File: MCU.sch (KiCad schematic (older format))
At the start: 27 parts, among them J15 RESET, J16 AVR-ISP-6, J17 WS2812, J18 SJ-43514-SMT, J4 AREF, J7 TYPE-C-31-M-12, SW1 EC11E, U1 ATmega32U4-AU, Y1 CSTNE16M0VH3L000R0

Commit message: Updated symbol library names
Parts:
- U1: symbol MCU_Atmel_ATMEGA:ATmega32U4-AU -> MCU_Microchip_ATmega:ATmega32U4-AU

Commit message: Added CUI connector lib
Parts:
- J16: value AVR-ISP-6 -> ISP
- J18: footprint (none) -> CUI:SJ-43514-SMT; symbol Connector:AudioJack4_Ground -> Connector:AudioJack4
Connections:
- net GND: no longer J18.G

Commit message: Added 3D models, prettied up silk
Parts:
- added D25: BAV70, Diode_SMD:D_SOD-323_HandSoldering, symbol Device:D_Small
- added D27: Red LED, symbol Device:LED_Small
- added R3: 220R, Resistor_SMD:R_0603_1608Metric_Pad1.05x0.95mm_HandSolder, symbol Device:R_Small
- added SW3: Reset, Button_Switch_SMD:SW_SPST_CK_RS282G05A3, symbol Switch:SW_Push
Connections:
- net Enc_A: now also U1.8 (PB0)
- net Enc_B: now also U1.1 (PE6)
- net GND: now also D27.1 (K), SW3.2; no longer SW1.S2
- net WS2812_out: now also U1.30 (PB6)
- net buzz: now also U1.31 (PC6)
- net row0: now also D25.2 (A)
- net ~reset: now also SW3.1
- net Enc_S1: now reaches U1.32 (PC7)
- net Enc_S1: now also SW1.S2
- net Enc_SW: no longer names the net of SW1.S1
- net Enc_SW: now also D25.1 (K)
- new net: D27.2 (A), R3.1
- new net DFU_LED: R3.2
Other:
- moved on the sheet: BZ1, BZ2, R12
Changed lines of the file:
@@
 EESchema Schematic File Version 4
-LIBS:MMboard1-cache
-EELAYER 30 0
+LIBS:mystic_split40-cache
+EELAYER 29 0
 EELAYER END
 $Descr A4 11693 8268
@@
 L Device:Buzzer BZ1
 U 1 1 5DD85748
-P 5175 5550
+P 5200 5925
 AR Path="/5DCB7F8C/5DD85748" Ref="BZ1"  Part="1"
 AR Path="/5E0F7128/5DD85748" Ref="BZ3"  Part="1"
-F 0 "BZ1" H 5328 5579 50  0000 L CNN
-F 1 "Buzzer_magnetic" H 5025 5375 50  0000 L CNN
-F 2 "Buzzer_Beeper:Buzzer_12x9.5RM7.6" V 5150 5650 50  0001 C CNN
-F 3 "~" V 5150 5650 50  0001 C CNN
-	1    5175 5550
+F 0 "BZ1" H 5353 5954 50  0000 L CNN
+F 1 "Buzzer_magnetic" H 5050 5750 50  0000 L CNN
+F 2 "Buzzer_Beeper:Buzzer_12x9.5RM7.6" V 5175 6025 50  0001 C CNN
+F 3 "~" V 5175 6025 50  0001 C CNN
+	1    5200 5925
 	1    0    0    -1
 $EndComp
@@
 L Device:Buzzer BZ2
 U 1 1 5DD864ED
-P 5175 6025
+P 5200 6400
 AR Path="/5DCB7F8C/5DD864ED" Ref="BZ2"  Part="1"
 AR Path="/5E0F7128/5DD864ED" Ref="BZ4"  Part="1"
-F 0 "BZ2" H 5327 6054 50  0000 L CNN
-F 1 "Buzzer_piezo" H 5025 6250 50  0000 L CNN
-F 2 "Buzzer_Beeper:Buzzer_Mallory_AST1109MLTRQ" V 5150 6125 50  0001 C CNN
-F 3 "~" V 5150 6125 50  0001 C CNN
-	1    5175 6025
+F 0 "BZ2" H 5352 6429 50  0000 L CNN
+F 1 "Buzzer_piezo" H 5050 6625 50  0000 L CNN
+F 2 "Buzzer_Beeper:Buzzer_Mallory_AST1109MLTRQ" V 5175 6500 50  0001 C CNN
+F 3 "~" V 5175 6500 50  0001 C CNN
+	1    5200 6400
 	1    0    0    -1
 $EndComp
@@
 L Device:R_Small R12
 U 1 1 5DD86EB4
-P 4975 5450
+P 5000 5825
 AR Path="/5DCB7F8C/5DD86EB4" Ref="R12"  Part="1"
 AR Path="/5E0F7128/5DD86EB4" Ref="R22"  Part="1"
-F 0 "R12" V 4825 5450 50  0000 C CNN
-F 1 "220R" V 4900 5450 50  0000 C CNN
-F 2 "Resistor_SMD:R_0603_1608Metric_Pad1.05x0.95mm_HandSolder" H 4975 5450 50  0001 C CNN
-F 3 "~" H 4975 5450 50  0001 C CNN
-	1    4975 5450
+F 0 "R12" V 4850 5825 50  0000 C CNN
+F 1 "220R" V 4925 5825 50  0000 C CNN
+F 2 "Resistor_SMD:R_0603_1608Metric_Pad1.05x0.95mm_HandSolder" H 5000 5825 50  0001 C CNN
+F 3 "~" H 5000 5825 50  0001 C CNN
+	1    5000 5825
 	0    1    1    0
 $EndComp
 Wire Wire Line
-	5075 5650 5000 5650
-Wire Wire Line
-	5000 5650 5000 6125
-Wire Wire Line
-	5000 6125 5075 6125
-Wire Wire Line
-	5075 5925 4825 5925
-Wire Wire Line
-	4825 5925 4825 5450
-Wire Wire Line
-	4825 5450 4875 5450
-Wire Wire Line
-	4825 5925 4775 5925
-Connection ~ 4825 5925
-Text Label 4775 5925 2    50   ~ 0
+	5100 6025 5025 6025
+Wire Wire Line
+	5025 6025 5025 6500
+Wire Wire Line
+	5025 6500 5100 6500
+Wire Wire Line
+	5100 6300 4850 6300
+Wire Wire Line
+	4850 6300 4850 5825
+Wire Wire Line
+	4850 5825 4900 5825
+Wire Wire Line
+	4850 6300 4800 6300
+Connection ~ 4850 6300
+Text Label 4800 6300 2    50   ~ 0
 buzz
 $Comp
 L power:GND #PWR0119
 U 1 1 5DD8FD53
-P 5000 6175
+P 5025 6550
 AR Path="/5DCB7F8C/5DD8FD53" Ref="#PWR0119"  Part="1"
 AR Path="/5E0F7128/5DD8FD53" Ref="#PWR0145"  Part="1"
-F 0 "#PWR0119" H 5000 5925 50  0001 C CNN
-F 1 "GND" H 5005 6002 50  0000 C CNN
-F 2 "" H 5000 6175 50  0001 C CNN
-F 3 "" H 5000 6175 50  0001 C CNN
-	1    5000 6175
-	1    0    0    -1
-$EndComp
-Wire Wire Line
-	5000 6175 5000 6125
-Connection ~ 5000 6125
+F 0 "#PWR0119" H 5025 6300 50  0001 C CNN
+F 1 "GND" H 5030 6377 50  0000 C CNN
+F 2 "" H 5025 6550 50  0001 C CNN
+F 3 "" H 5025 6550 50  0001 C CNN
+	1    5025 6550
+	1    0    0    -1
+$EndComp
+Wire Wire Line
+	5025 6550 5025 6500
+Connection ~ 5025 6500
 $Comp
 L Connector_Generic:Conn_01x03 J17
@@
 Text Label 4050 6225 2    50   ~ 0
 WS2812_out
-Text Label 3275 7100 0    50   ~ 0
+Text Label 3450 7100 2    50   ~ 0
 SDA
-Text Label 3275 7000 0    50   ~ 0
+Text Label 3450 7000 2    50   ~ 0
 SCL
 Text Label 3900 7000 2    50   ~ 0
@@
 	4850 1850 4750 1850
 Wire Wire Line
-	3450 7000 3225 7000
-Wire Wire Line
-	3225 7100 3450 7100
-Text HLabel 3225 7000 0    50   UnSpc ~ 0
+	3450 7000 3300 7000
+Wire Wire Line
+	3300 7100 3450 7100
+Text HLabel 3300 7000 0    50   UnSpc ~ 0
 SCL
-Text HLabel 3225 7100 0    50   UnSpc ~ 0
+Text HLabel 3300 7100 0    50   UnSpc ~ 0
 SDA
 $Comp
@@
 	1    0    0    -1
 $EndComp
-Text Label 4825 7450 2    50   ~ 0
-Enc_B
-Text Label 4825 7250 2    50   ~ 0
-Enc_A
-Text Label 5425 7250 0    50   ~ 0
-Enc_SW
-$Comp
-L power:GND #PWR0158
-U 1 1 5E3FD1C4
-P 5475 7500
-AR Path="/5DCB7F8C/5E3FD1C4" Ref="#PWR0158"  Part="1"
-AR Path="/5E0F7128/5E3FD1C4" Ref="#PWR0160"  Part="1"
-F 0 "#PWR0158" H 5475 7250 50  0001 C CNN
-F 1 "GND" H 5480 7327 50  0000 C CNN
-F 2 "" H 5475 7500 50  0001 C CNN
-F 3 "" H 5475 7500 50  0001 C CNN
-	1    5475 7500
-	1    0    0    -1
-$EndComp
-Wire Wire Line
-	5475 7500 5475 7450
-Wire Wire Line
-	5475 7450 5425 7450
+Text Label 5425 7450 0    50   ~ 0
+Enc_S1
 $Comp
 L power:GND #PWR0159
@@
 Text Notes 2750 4925 0    50   ~ 0
 I/O
-Text Label 5425 2575 2    50   ~ 0
+Text Label 4850 3350 0    50   ~ 0
+Enc_B
+Wire Wire Line
+	3850 7200 3850 7250
+Text Label 4850 1750 0    50   ~ 0
+WS2812_out
+Text Label 4850 1150 0    50   ~ 0
 Enc_A
-Wire Wire Line
-	3850 7200 3850 7250
+Text Label 4850 2050 0    50   ~ 0
+buzz
+Wire Wire Line
+	4850 2050 4750 2050
+Wire Wire Line
+	4850 3350 4750 3350
+Wire Wire Line
+	4850 1150 4750 1150
+Text Label 4850 2150 0    50   ~ 0
+Enc_S1
+Wire Wire Line
+	4850 2150 4750 2150
+$Comp
+L Device:D_Small D25
+U 1 1 5DC9668D
+P 5450 7125
+AR Path="/5DCB7F8C/5DC9668D" Ref="D25"  Part="1"
+AR Path="/5E0F7128/5DC9668D" Ref="D26"  Part="1"
+F 0 "D25" V 5525 7150 50  0000 L CNN
+F 1 "BAV70" V 5375 7150 50  0000 L CNN
+F 2 "Diode_SMD:D_SOD-323_HandSoldering" V 5450 7125 50  0001 C CNN
+F 3 "~" V 5450 7125 50  0001 C CNN
+	1    5450 7125
+	0    1    -1   0
+$EndComp
+Text HLabel 5450 7025 1    50   Input ~ 0
+row0
+Wire Wire Line
+	5425 7250 5450 7250
+Wire Wire Line
+	5450 7250 5450 7225
+$Comp
+L Switch:SW_Push SW3
+U 1 1 5DCEA8F4
+P 5125 5375
+AR Path="/5DCB7F8C/5DCEA8F4" Ref="SW3"  Part="1"
+AR Path="/5E0F7128/5DCEA8F4" Ref="SW4"  Part="1"
+F 0 "SW3" H 5125 5660 50  0000 C CNN
+F 1 "Reset" H 5125 5569 50  0000 C CNN
+F 2 "Button_Switch_SMD:SW_SPST_CK_RS282G05A3" H 5125 5575 50  0001 C CNN
+F 3 "~" H 5125 5575 50  0001 C CNN
+	1    5125 5375
+	1    0    0    -1
+$EndComp
+$Comp
+L power:GND #PWR0158
+U 1 1 5DD09F85
+P 5375 5425
+AR Path="/5DCB7F8C/5DD09F85" Ref="#PWR0158"  Part="1"
+AR Path="/5E0F7128/5DD09F85" Ref="#PWR0160"  Part="1"
+F 0 "#PWR0158" H 5375 5175 50  0001 C CNN
+F 1 "GND" H 5380 5252 50  0000 C CNN
+F 2 "" H 5375 5425 50  0001 C CNN
+F 3 "" H 5375 5425 50  0001 C CNN
+	1    5375 5425
+	1    0    0    -1
+$EndComp
+Text Label 4875 5375 2    50   ~ 0
+~reset
+Wire Wire Line
+	4875 5375 4925 5375
+Wire Wire Line
+	5325 5375 5375 5375
+Wire Wire Line
+	5375 5375 5375 5425
+Wire Wire Line
+	4850 1750 4750 1750
+Text Label 4825 7450 2    50   ~ 0
+Enc_B
+Text Label 4825 7250 2    50   ~ 0
+Enc_A
+$Comp
+L Device:LED_Small D27
+U 1 1 5DD960C9
+P 2925 7150
+AR Path="/5DCB7F8C/5DD960C9" Ref="D27"  Part="1"
+AR Path="/5E0F7128/5DD960C9" Ref="D28"  Part="1"
+F 0 "D27" V 2850 7050 50  0000 C CNN
+F 1 "Red LED" H 2875 7275 50  0000 C CNN
+F 2 "" V 2925 7150 50  0001 C CNN
+F 3 "~" V 2925 7150 50  0001 C CNN
+	1    2925 7150
+	0    -1   -1   0
+$EndComp
+$Comp
+L power:GND #PWR0162
+U 1 1 5DD9710C
+P 2925 7250
+AR Path="/5DCB7F8C/5DD9710C" Ref="#PWR0162"  Part="1"
+AR Path="/5E0F7128/5DD9710C" Ref="#PWR0163"  Part="1"
+F 0 "#PWR0162" H 2925 7000 50  0001 C CNN
+F 1 "GND" V 2930 7122 50  0000 R CNN
+F 2 "" H 2925 7250 50  0001 C CNN
+F 3 "" H 2925 7250 50  0001 C CNN
+	1    2925 7250
+	1    0    0    -1
+$EndComp
+$Comp
+L Device:R_Small R3
+U 1 1 5DD99298
+P 2925 6950
+AR Path="/5DCB7F8C/5DD99298" Ref="R3"  Part="1"
+AR Path="/5E0F7128/5DD99298" Ref="R4"  Part="1"
+F 0 "R3" V 2850 6775 50  0000 C CNN
+F 1 "220R" V 2850 6950 50  0000 C CNN
+F 2 "Resistor_SMD:R_0603_1608Metric_Pad1.05x0.95mm_HandSolder" H 2925 6950 50  0001 C CNN
+F 3 "~" H 2925 6950 50  0001 C CNN
+	1    2925 6950
+	-1   0    0    1
+$EndComp
+Wire Wire Line
+	2925 6850 2925 6675
+Wire Wire Line
+	2925 6675 2850 6675
+Text Label 2850 6675 0    50   ~ 0
+DFU_LED
 $EndSCHEMATC

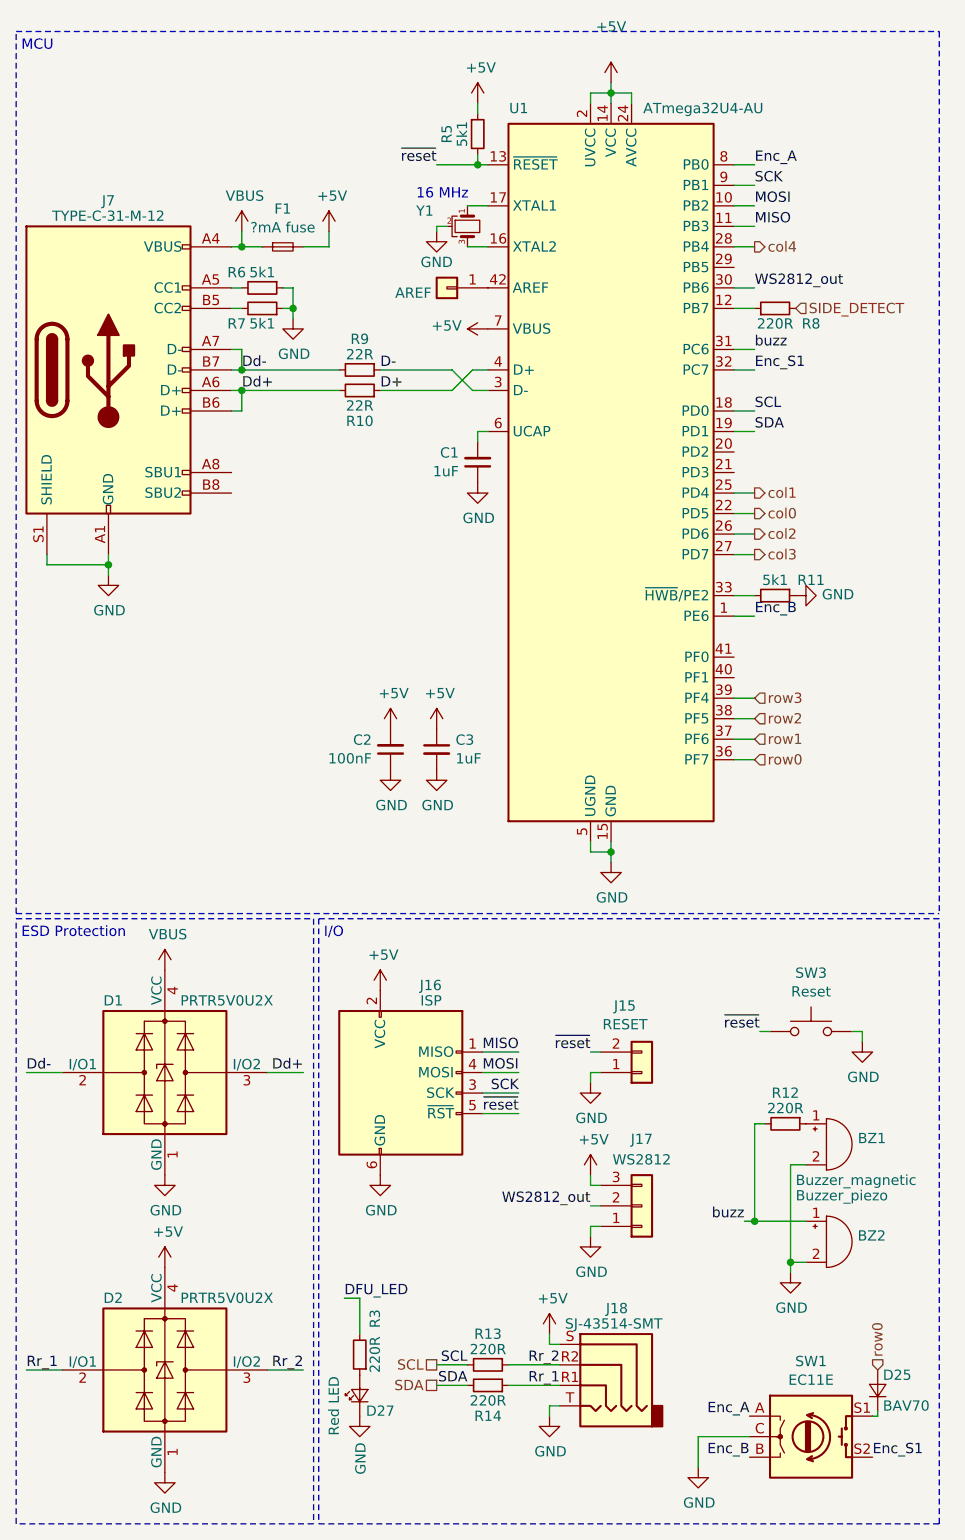
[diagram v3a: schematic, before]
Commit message: Copied left half layout to right components
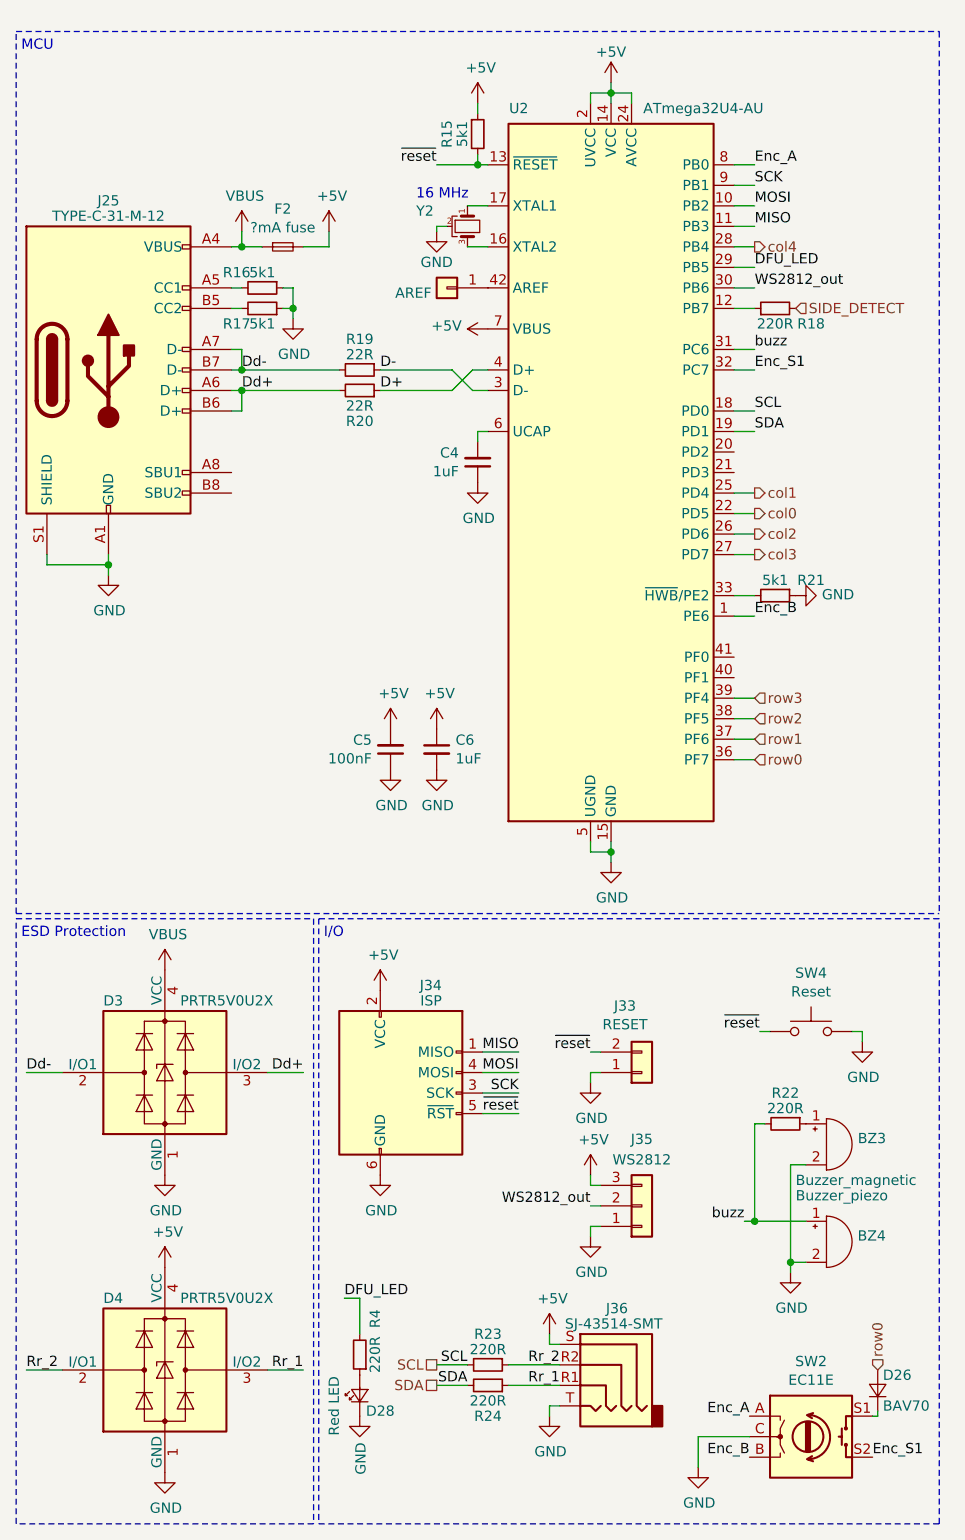
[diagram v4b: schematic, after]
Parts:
- D27: footprint (none) -> LED_SMD:LED_0805_2012Metric_Pad1.15x1.40mm_HandSolder
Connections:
- net DFU_LED: now also U1.29 (PB5)
- net Rr_1: now also D2.3 (I/O2); no longer D2.2 (I/O1)
- net Rr_2: now also D2.2 (I/O1); no longer D2.3 (I/O2)

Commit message: Finished right-side, added BOM
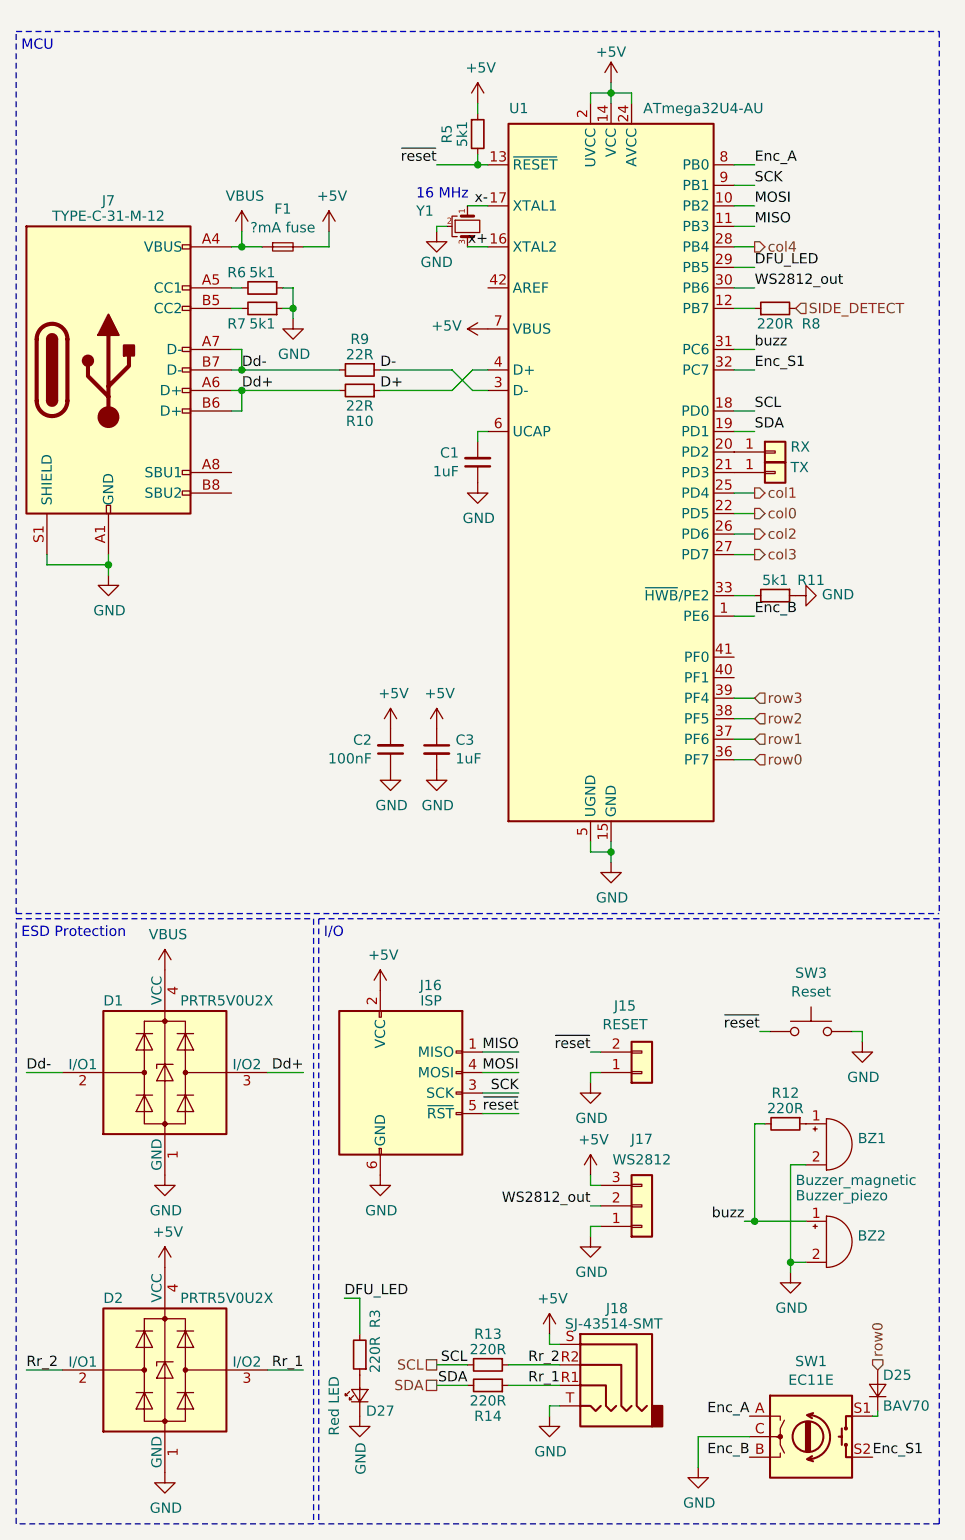
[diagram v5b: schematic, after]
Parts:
- removed J4: AREF, TestPoint:TestPoint_Pad_D1.0mm, symbol Connector_Generic:Conn_01x01
- added J1: RX, TestPoint:TestPoint_Pad_D1.0mm, symbol Connector_Generic:Conn_01x01
- added J2: TX, TestPoint:TestPoint_Pad_D1.0mm, symbol Connector_Generic:Conn_01x01
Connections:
- net x+: now reaches U1.16 (XTAL2), Y1.3
- net x-: now reaches U1.17 (XTAL1), Y1.1
- net at U1.20 (PD2): now also J1.1 (Pin_1)
- net at U1.21 (PD3): now also J2.1 (Pin_1)

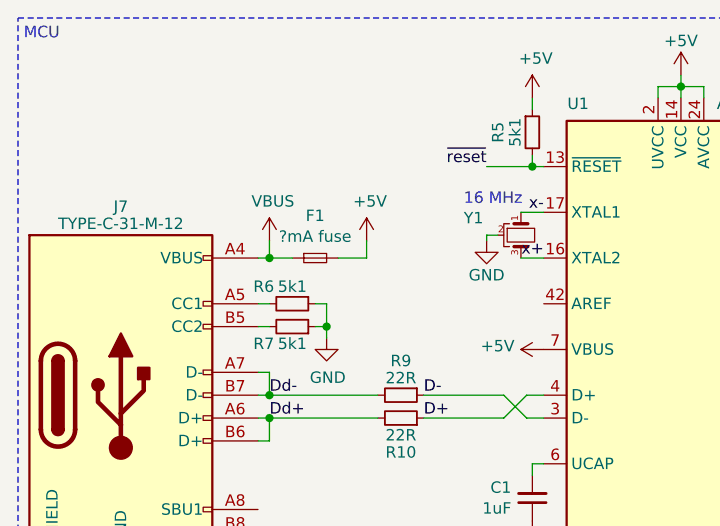
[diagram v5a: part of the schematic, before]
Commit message: Fixed up silkscreen
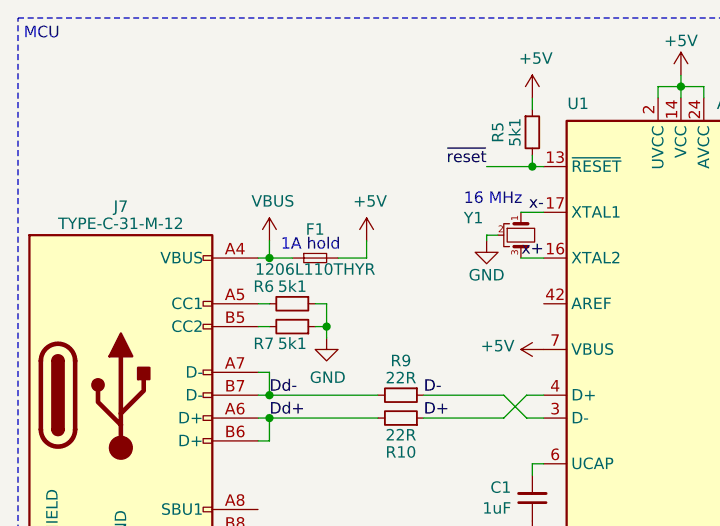
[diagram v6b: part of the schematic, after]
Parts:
- F1: value ?mA fuse -> 1206L110THYR
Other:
- note added: "1A hold"
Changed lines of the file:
@@
 AR Path="/5DCB7F8C/5DCF5E76" Ref="F1"  Part="1"
 AR Path="/5E0F7128/5DCF5E76" Ref="F2"  Part="1"
-F 0 "F1" H 2550 1735 50  0000 C CNN
-F 1 "?mA fuse" H 2550 1644 50  0000 C CNN
+F 0 "F1" H 2550 1675 50  0000 C CNN
+F 1 "1206L110THYR" H 2550 1500 50  0000 C CNN
 F 2 "Fuse:Fuse_1206_3216Metric_Pad1.42x1.75mm_HandSolder" H 2550 1550 50  0001 C CNN
 F 3 "~" H 2550 1550 50  0001 C CNN
@@
 	1    0    0    -1
 $EndComp
+Text Notes 2400 1525 0    50   ~ 0
+1A hold
 $EndSCHEMATC
